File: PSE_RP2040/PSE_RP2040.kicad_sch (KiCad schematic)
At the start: 77 parts, among them IC1 AT25SF128A-SHB-T, IC2 SAM-M8Q-0, J1 USB_B, J2 USB_B_Micro, J3 Conn_01x02, U1 RP2040

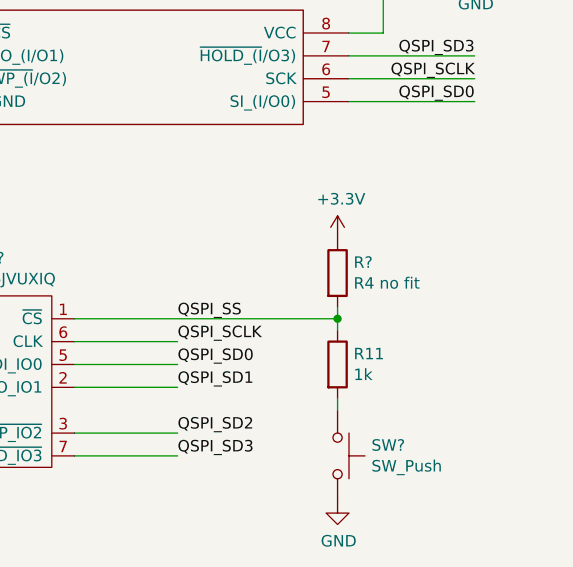
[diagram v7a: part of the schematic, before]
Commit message: modifiche schematico
cancellata sezione alimentazione non più necessaria (usiamo switching del poe)
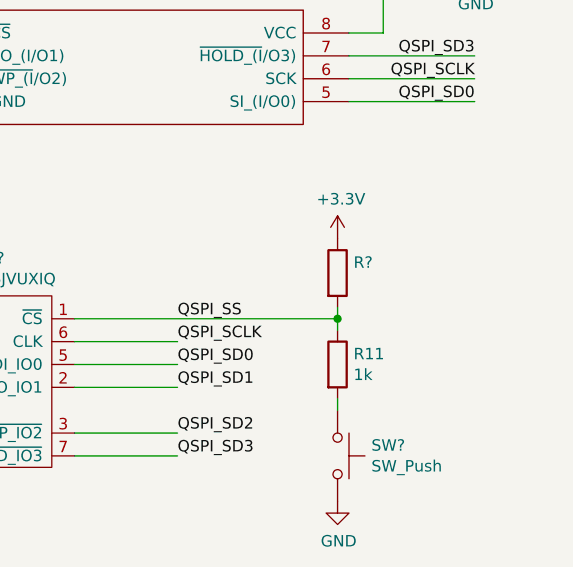
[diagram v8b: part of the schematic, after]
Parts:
- R?: value R4 no fit -> (none)
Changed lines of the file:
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@@
       (effects (font (size 1.27 1.27)) (justify left))
     )
-    (property "Value" "R4 no fit" (id 1) (at 385.318 70.993 0)
+    (property "Value" "" (id 1) (at 385.318 70.993 0)
       (effects (font (size 1.27 1.27)) (justify left))
     )
@@
   )
   (symbol_instances
-    (path "/cfa038c0-a49f-45bf-b6e3-72692695ea2c/e64fbc32-e3ec-4a25-ad5c-93550782d84a"
-      (reference "#FLG?") (unit 1) (value "PWR_FLAG") (footprint "")
-    )
     (path "/00000000-0000-0000-0000-0000622de161"
       (reference "#PWR0101") (unit 1) (value "GND") (footprint "")
@@
       (reference "#PWR?") (unit 1) (value "GND") (footprint "")
     )
-    (path "/cfa038c0-a49f-45bf-b6e3-72692695ea2c/0de2920a-b93a-4338-bc95-dfbb6050b146"
-      (reference "#PWR?") (unit 1) (value "GND") (footprint "")
-    )
     (path "/0df40f43-d59d-4bf1-b2e8-22aead9235c5"
       (reference "#PWR?") (unit 1) (value "GND") (footprint "")
@@
     )
     (path "/17312dee-f5df-46db-8d31-512af4ff3e57"
-      (reference "#PWR?") (unit 1) (value "GND") (footprint "")
-    )
-    (path "/cfa038c0-a49f-45bf-b6e3-72692695ea2c/23826232-67f3-4af4-8ca5-050eb6295e7e"
       (reference "#PWR?") (unit 1) (value "GND") (footprint "")
     )
@@
       (reference "#PWR?") (unit 1) (value "+3V3") (footprint "")
     )
-    (path "/cfa038c0-a49f-45bf-b6e3-72692695ea2c/4538e17b-0829-4ec8-b384-5f499d7f0685"
-      (reference "#PWR?") (unit 1) (value "GND") (footprint "")
-    )
-    (path "/cfa038c0-a49f-45bf-b6e3-72692695ea2c/48c2ae34-9dd2-42de-a36a-f7eafa7fc89d"
-      (reference "#PWR?") (unit 1) (value "+5V") (footprint "")
-    )
     (path "/cfa038c0-a49f-45bf-b6e3-72692695ea2c/5aff567d-c33e-45a9-a80f-fb9143f0218c"
       (reference "#PWR?") (unit 1) (value "GND") (footprint "")
@@
     )
     (path "/7ad72399-619d-4ac7-a5cd-378f19beec55"
-      (reference "#PWR?") (unit 1) (value "GND") (footprint "")
-    )
-    (path "/cfa038c0-a49f-45bf-b6e3-72692695ea2c/8181bb91-58d4-45b0-ac7d-ea3d99e7998a"
       (reference "#PWR?") (unit 1) (value "GND") (footprint "")
     )
@@
       (reference "#PWR?") (unit 1) (value "GND") (footprint "")
     )
-    (path "/cfa038c0-a49f-45bf-b6e3-72692695ea2c/919f7355-7a99-4fca-aa5a-f39e752a9855"
-      (reference "#PWR?") (unit 1) (value "GND") (footprint "")
-    )
     (path "/cfa038c0-a49f-45bf-b6e3-72692695ea2c/92cee0fa-2dfc-4b27-8a10-6cd77058ef93"
       (reference "#PWR?") (unit 1) (value "GND") (footprint "")
-    )
-    (path "/cfa038c0-a49f-45bf-b6e3-72692695ea2c/9b282d6d-6bbb-4727-b85c-7b00ccc25fbe"
-      (reference "#PWR?") (unit 1) (value "GND") (footprint "")
-    )
-    (path "/cfa038c0-a49f-45bf-b6e3-72692695ea2c/9bf79a59-ff93-41a4-9b89-ede73a9f9f3d"
-      (reference "#PWR?") (unit 1) (value "+5V") (footprint "")
     )
     (path "/9f7c4831-66d9-40e5-8432-dcfc50b42594"
@@
       (reference "#PWR?") (unit 1) (value "GND") (footprint "")
     )
-    (path "/cfa038c0-a49f-45bf-b6e3-72692695ea2c/c6f68e7a-6c0e-4e5c-a066-1a168b540926"
-      (reference "#PWR?") (unit 1) (value "+3.3V") (footprint "")
-    )
-    (path "/cfa038c0-a49f-45bf-b6e3-72692695ea2c/d0b55dad-b1c6-4972-a435-47841fbb24d4"
-      (reference "#PWR?") (unit 1) (value "+3.3V") (footprint "")
-    )
     (path "/e1040306-7511-4d2a-b26e-ad7e54e19327"
       (reference "#PWR?") (unit 1) (value "GND") (footprint "")
@@
     )
     (path "/f0043f6b-c716-4e07-827d-41510609795a"
-      (reference "#PWR?") (unit 1) (value "GND") (footprint "")
-    )
-    (path "/cfa038c0-a49f-45bf-b6e3-72692695ea2c/f24b4d57-c7d9-461b-943a-06fd3a94a09f"
       (reference "#PWR?") (unit 1) (value "GND") (footprint "")
     )
@@
       (reference "C18") (unit 1) (value "2u2") (footprint "")
     )
-    (path "/cfa038c0-a49f-45bf-b6e3-72692695ea2c/09139a82-cf5b-42e4-b875-13118e1a3e07"
-      (reference "C?") (unit 1) (value "100n") (footprint "")
-    )
     (path "/306d58a4-774e-4597-a070-c0199d91c582"
       (reference "C?") (unit 1) (value "C") (footprint "")
@@
       (reference "C?") (unit 1) (value "100n") (footprint "")
     )
-    (path "/cfa038c0-a49f-45bf-b6e3-72692695ea2c/52ddc23e-bf38-4225-99d2-f6c4bb5622a5"
-      (reference "C?") (unit 1) (value "47u") (footprint "")
-    )
     (path "/cfa038c0-a49f-45bf-b6e3-72692695ea2c/56d29c62-b2b5-4ace-9fab-a8e69049c888"
       (reference "C?") (unit 1) (value "100u") (footprint "")
@@
       (reference "C?") (unit 1) (value "C") (footprint "")
     )
-    (path "/cfa038c0-a49f-45bf-b6e3-72692695ea2c/8b7564a2-0f77-4d7a-9dcf-b285521d1809"
-      (reference "C?") (unit 1) (value "47u") (footprint "")
-    )
     (path "/cfa038c0-a49f-45bf-b6e3-72692695ea2c/909b0597-d57d-41a2-8a46-e89172577714"
       (reference "C?") (unit 1) (value "100n 100v") (footprint "")
@@
       (reference "C?") (unit 1) (value "470p") (footprint "")
     )
-    (path "/cfa038c0-a49f-45bf-b6e3-72692695ea2c/e203136f-79aa-4f0b-8f75-57b900addf65"
-      (reference "C?") (unit 1) (value "1u") (footprint "")
-    )
     (path "/cfa038c0-a49f-45bf-b6e3-72692695ea2c/efd1443e-8baa-4824-aa5d-0ede8032d217"
       (reference "C?") (unit 1) (value "100n 100v") (footprint "")
@@
       (reference "D?") (unit 1) (value "LED") (footprint "")
     )
-    (path "/cfa038c0-a49f-45bf-b6e3-72692695ea2c/1e0cfdb2-d3f2-4bfd-bfd4-8dae3451acec"
-      (reference "D?") (unit 1) (value "MBR1020VL") (footprint "Diode_SMD:D_SOD-123F")
-    )
     (path "/cfa038c0-a49f-45bf-b6e3-72692695ea2c/5a60a596-f969-4048-b9f0-6c28b54abd9a"
       (reference "D?") (unit 1) (value "MBR1020VL") (footprint "Diode_SMD:D_SOD-123F")
@@
       (reference "D?") (unit 1) (value "D_Bridge_+-AA") (footprint "")
     )
-    (path "/cfa038c0-a49f-45bf-b6e3-72692695ea2c/91a6fff7-fe6a-4062-b3d1-93d0d31e40ac"
-      (reference "D?") (unit 1) (value "MBR1020VL") (footprint "Diode_SMD:D_SOD-123F")
-    )
     (path "/96cbc19c-9e01-406e-a91b-5164df994b39"
       (reference "D?") (unit 1) (value "D_Bridge_+-AA") (footprint "")
@@
       (reference "L?") (unit 1) (value "L") (footprint "")
     )
-    (path "/cfa038c0-a49f-45bf-b6e3-72692695ea2c/e67dc1b5-552d-4a86-b7fc-d4910c872ce8"
-      (reference "L?") (unit 1) (value "2U2") (footprint "")
-    )
     (path "/00000000-0000-0000-0000-0000624df8fb"
       (reference "Q?") (unit 1) (value "DTC114Y") (footprint "")
@@
     )
     (path "/00000000-0000-0000-0000-00006235b6f7"
-      (reference "R?") (unit 1) (value "R4 no fit") (footprint "")
+      (reference "R?") (unit 1) (value "R4 no fit (o 10k)") (footprint "")
     )
     (path "/00000000-0000-0000-0000-000062511dac"
@@
       (reference "R?") (unit 1) (value "R") (footprint "")
     )
-    (path "/cfa038c0-a49f-45bf-b6e3-72692695ea2c/4274cf26-61f5-4ef2-a9b4-fb1d1701011a"
-      (reference "R?") (unit 1) (value "100k") (footprint "")
-    )
     (path "/cfa038c0-a49f-45bf-b6e3-72692695ea2c/48ea6c06-49df-4397-8f17-d45fed47211b"
       (reference "R?") (unit 1) (value "330") (footprint "")
@@
       (reference "R?") (unit 1) (value "10k") (footprint "")
     )
-    (path "/cfa038c0-a49f-45bf-b6e3-72692695ea2c/ca1016c1-8341-4511-b52b-e464eb978bc0"
-      (reference "R?") (unit 1) (value "100k") (footprint "")
-    )
     (path "/d16bddef-f756-4c62-bafe-b7696d4d053a"
       (reference "R?") (unit 1) (value "49,9") (footprint "")
@@
       (reference "U?") (unit 1) (value "TPS2375-1") (footprint "Package_SO:TSSOP-8_4.4x3mm_P0.65mm")
     )
-    (path "/cfa038c0-a49f-45bf-b6e3-72692695ea2c/a41dacfc-f8a7-4469-844b-e8f5837274cc"
-      (reference "U?") (unit 1) (value "MCP1703A-3302_SOT23") (footprint "Package_TO_SOT_SMD:SOT-23")
-    )
-    (path "/cfa038c0-a49f-45bf-b6e3-72692695ea2c/c3f84489-e5f3-423a-835e-8ee6516c9c28"
-      (reference "U?") (unit 1) (value "RT6150A_B") (footprint "")
-    )
     (path "/e387b3da-1b1e-4084-83ba-3fa8e6c7f673"
